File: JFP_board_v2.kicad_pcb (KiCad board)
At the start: 2 copper layers, 52.5 x 51.5 mm, 84 parts, among them J1 SPI2 external, J2 RX header, J3 I2C2 external, J4 UART4 external, J5 SWD conn, J6 ESC conn, J7 918-418K2023S40001, Q1 AO3400A, SW1 BOOT0, U1 TPS5430DDAR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

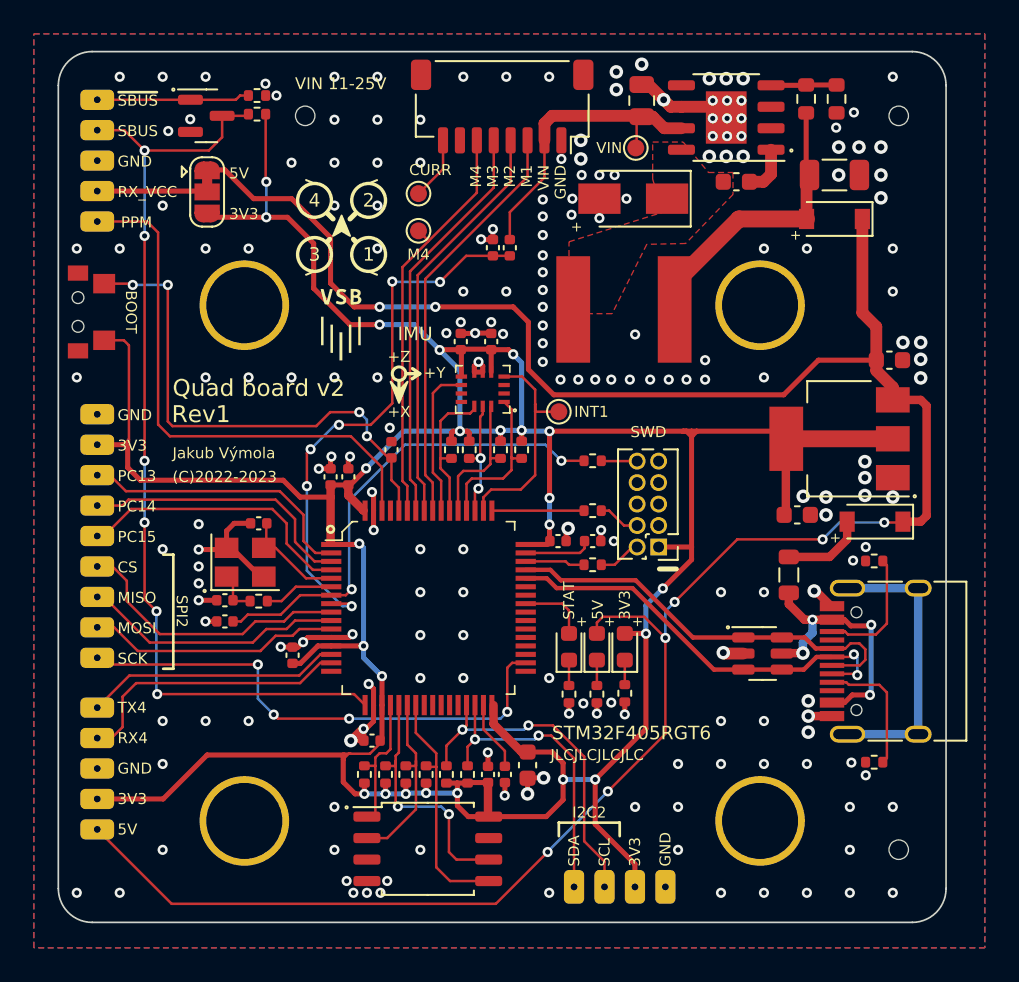
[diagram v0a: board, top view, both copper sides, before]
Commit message: Added HP203B pressure sensor
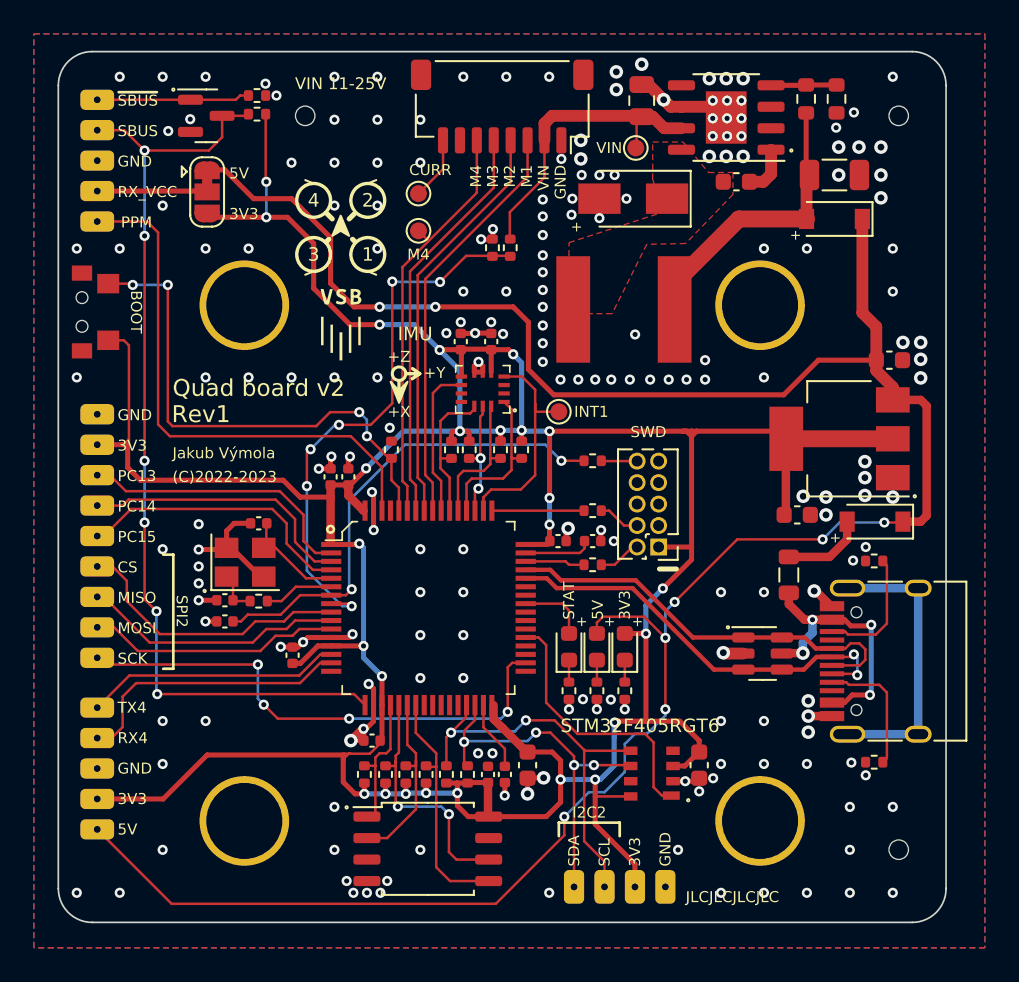
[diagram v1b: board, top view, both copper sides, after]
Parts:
- added C20: 4.7uF, Capacitor_SMD:C_0603_1608Metric, F.Cu at (163.4, 92.7)
- added U7: HP203B, _custom_footprints:LGA-8_3.6x3.8x0.9P, F.Cu at (160.6, 93.2)
- R10, R23, R24: footprint Capacitor_SMD:C_0402_1005Metric -> Resistor_SMD:R_0402_1005Metric
- R13, R15: value 100k -> 10k
- moved SW1 0.24 mm to (126.9, 65.9)
- moved R7 0.20 mm to (157.3, 88.3)
- moved R9 0.20 mm to (155.7, 88.3)
- moved R8 0.15 mm to (159.0, 88.3)
- moved REFQUAD 0.05 mm to (142.2, 60.9)
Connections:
- U3 pad 37: unconnected-(U3-Pad37) -> HP203B_INT1
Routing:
- net HP203B_INT1: track 0.00 -> 16.0 mm
- net +3V3: track 225.7 -> 234.8 mm, vias 24 -> 25
- net I2C2_SDA: track 17.9 -> 22.3 mm, vias 2 -> 4
- net I2C2_SCL: track 20.3 -> 24.3 mm
- net +5V: track 139.2 -> 140.1 mm
- net GND: track 43.7 -> 44.3 mm, vias 202 -> 201

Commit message: Production files
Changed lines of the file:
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@@
   (setup
     (stackup
-      (layer "F.SilkS" (type "Top Silk Screen"))
+      (layer "F.SilkS" (type "Top Silk Screen") (color "White"))
       (layer "F.Paste" (type "Top Solder Paste"))
-      (layer "F.Mask" (type "Top Solder Mask") (thickness 0.01))
+      (layer "F.Mask" (type "Top Solder Mask") (color "Green") (thickness 0.01))
       (layer "F.Cu" (type "copper") (thickness 0.035))
       (layer "dielectric 1" (type "core") (thickness 1.51) (material "FR4") (epsilon_r 4.5) (loss_tangent 0.02))
       (layer "B.Cu" (type "copper") (thickness 0.035))
-      (layer "B.Mask" (type "Bottom Solder Mask") (thickness 0.01))
+      (layer "B.Mask" (type "Bottom Solder Mask") (color "Green") (thickness 0.01))
       (layer "B.Paste" (type "Bottom Solder Paste"))
-      (layer "B.SilkS" (type "Bottom Silk Screen"))
+      (layer "B.SilkS" (type "Bottom Silk Screen") (color "White"))
       (copper_finish "None")
       (dielectric_constraints no)
@@
     (pad_to_mask_clearance 0.05)
     (pcbplotparams
-      (layerselection 0x00010fc_ffffffff)
+      (layerselection 0x000d0fc_ffffffff)
       (disableapertmacros false)
       (usegerberextensions false)
@@
       (svguseinch false)
       (svgprecision 6)
-      (excludeedgelayer true)
+      (excludeedgelayer false)
       (plotframeref false)
       (viasonmask false)
@@
       (sketchpadsonfab false)
       (subtractmaskfromsilk false)
-      (outputformat 1)
+      (outputformat 4)
       (mirror false)
       (drillshape 0)
       (scaleselection 1)
-      (outputdirectory "assembly/")
+      (outputdirectory "schematic/")
     )
   )
@@
     (effects (font (size 0.65 0.65) (thickness 0.16)) (justify left))
   )
-  (gr_text "VIN 11-25V" (at 142.2 52.4) (layer "F.SilkS")
+  (gr_text "VIN 11-25V" (at 142.225 52.85) (layer "F.SilkS")
     (effects (font (size 0.7 0.7) (thickness 0.16)))
   )
@@
     (effects (font (size 1 1) (thickness 0.2)) (justify left))
   )
-  (gr_text "JLCJLCJLCJLC" (at 162.6 100.5) (layer "F.SilkS")
+  (gr_text "JLCJLCJLCJLC" (at 162.625 99.6) (layer "F.SilkS")
     (effects (font (size 0.65 0.65) (thickness 0.16)) (justify left))
   )
@@
   (segment (start 141.64 84.65) (end 139.75 84.65) (width 0.15) (layer "F.Cu") (net 21))
   (segment (start 138.35 85.05) (end 137.45 85.95) (width 0.15) (layer "F.Cu") (net 21))
-  (segment (start 137.65025 89.12475) (end 138.4755 89.95) (width 0.15) (layer "F.Cu") (net 22))
+  (segment (start 138.4755 89.95) (end 142.7 89.95) (width 0.15) (layer "F.Cu") (net 22))
+  (segment (start 137.88775 89.36225) (end 138.4755 89.95) (width 0.15) (layer "F.Cu") (net 22))
   (segment (start 152.34 86.65) (end 153.14 86.65) (width 0.15) (layer "F.Cu") (net 22))
   (segment (start 128.2 86.75) (end 137.3 86.75) (width 0.15) (layer "F.Cu") (net 22))
   (segment (start 152.075 89.55) (end 152.075 86.915) (width 0.15) (layer "F.Cu") (net 22))
-  (segment (start 138.4755 89.95) (end 142.7 89.95) (width 0.15) (layer "F.Cu") (net 22))
   (segment (start 152.075 86.915) (end 152.34 86.65) (width 0.15) (layer "F.Cu") (net 22))
   (via (at 152.075 89.55) (size 0.6) (drill 0.3) (layers "F.Cu" "B.Cu") (net 22))
-  (via (at 137.65025 89.12475) (size 0.6) (drill 0.3) (layers "F.Cu" "B.Cu") (net 22))
+  (via (at 137.88775 89.36225) (size 0.6) (drill 0.3) (layers "F.Cu" "B.Cu") (net 22))
   (via (at 137.3 86.75) (size 0.6) (drill 0.3) (layers "F.Cu" "B.Cu") (net 22))
   (via (at 142.7 89.95) (size 0.6) (drill 0.3) (layers "F.Cu" "B.Cu") (net 22))
   (segment (start 152.075 89.55) (end 151.675 89.95) (width 0.15) (layer "B.Cu") (net 22))
-  (segment (start 137.65025 89.12475) (end 137.3 88.7745) (width 0.15) (layer "B.Cu") (net 22))
   (segment (start 137.3 88.7745) (end 137.3 86.75) (width 0.15) (layer "B.Cu") (net 22))
+  (segment (start 137.88775 89.36225) (end 137.3 88.7745) (width 0.15) (layer "B.Cu") (net 22))
   (segment (start 151.675 89.95) (end 142.7 89.95) (width 0.15) (layer "B.Cu") (net 22))
   (segment (start 139 78.4) (end 138.15 77.55) (width 0.15) (layer "F.Cu") (net 23))
@@
   (segment (start 142.8 73.25) (end 144.64 75.09) (width 0.15) (layer "F.Cu") (net 27))
   (segment (start 144.64 75.09) (end 144.64 77.65) (width 0.15) (layer "F.Cu") (net 27))
+  (segment (start 143.215 88.725) (end 143.64 89.15) (width 0.15) (layer "F.Cu") (net 28))
   (segment (start 131.306233 83.6) (end 130.6 82.893767) (width 0.15) (layer "F.Cu") (net 28))
   (segment (start 136.64 54.3) (end 135.1875 54.3) (width 0.15) (layer "F.Cu") (net 28))
   (segment (start 130.6 74.7) (end 130.6 61.4) (width 0.15) (layer "F.Cu") (net 28))
-  (segment (start 143.64 89.15) (end 142.99 88.5) (width 0.15) (layer "F.Cu") (net 28))
   (segment (start 130.6 56.35) (end 134.4 56.35) (width 0.15) (layer "F.Cu") (net 28))
   (segment (start 129.4 55.15) (end 130.6 56.35) (width 0.15) (layer "F.Cu") (net 28))
   (segment (start 135.1875 55.5625) (end 135.1875 54.3) (width 0.15) (layer "F.Cu") (net 28))
-  (segment (start 142.99 88.5) (end 131.35 88.5) (width 0.15) (layer "F.Cu") (net 28))
+  (segment (start 131.45 88.725) (end 143.215 88.725) (width 0.15) (layer "F.Cu") (net 28))
   (segment (start 127.8 55.15) (end 129.4 55.15) (width 0.15) (layer "F.Cu") (net 28))
   (segment (start 134.4 56.35) (end 135.1875 55.5625) (width 0.15) (layer "F.Cu") (net 28))
   (segment (start 130.6 82.893767) (end 130.6 78.35) (width 0.15) (layer "F.Cu") (net 28))
+  (segment (start 131.4 88.775) (end 131.45 88.725) (width 0.15) (layer "F.Cu") (net 28))
   (via (at 130.6 78.35) (size 0.6) (drill 0.3) (layers "F.Cu" "B.Cu") (net 28))
   (via (at 131.306233 83.6) (size 0.6) (drill 0.3) (layers "F.Cu" "B.Cu") (net 28))
@@
   (via (at 130.6 56.35) (size 0.6) (drill 0.3) (layers "F.Cu" "B.Cu") (net 28))
   (via (at 130.6 61.4) (size 0.6) (drill 0.3) (layers "F.Cu" "B.Cu") (net 28))
-  (via (at 131.35 88.5) (size 0.6) (drill 0.3) (layers "F.Cu" "B.Cu") (net 28))
+  (via (at 131.4 88.775) (size 0.6) (drill 0.3) (layers "F.Cu" "B.Cu") (net 28))
+  (segment (start 131.3 83.606233) (end 131.306233 83.6) (width 0.15) (layer "B.Cu") (net 28))
   (segment (start 130.6 56.35) (end 130.6 61.4) (width 0.15) (layer "B.Cu") (net 28))
-  (segment (start 131.35 88.5) (end 131.3 88.45) (width 0.15) (layer "B.Cu") (net 28))
+  (segment (start 131.3 88.675) (end 131.3 83.606233) (width 0.15) (layer "B.Cu") (net 28))
+  (segment (start 131.4 88.775) (end 131.3 88.675) (width 0.15) (layer "B.Cu") (net 28))
   (segment (start 130.6 74.7) (end 130.6 78.35) (width 0.15) (layer "B.Cu") (net 28))
-  (segment (start 131.3 88.45) (end 131.3 83.606233) (width 0.15) (layer "B.Cu") (net 28))
-  (segment (start 131.3 83.606233) (end 131.306233 83.6) (width 0.15) (layer "B.Cu") (net 28))
   (segment (start 136 53.35) (end 136.25 53.1) (width 0.15) (layer "F.Cu") (net 29))
   (segment (start 136.25 53.1) (end 136.74 53.1) (width 0.15) (layer "F.Cu") (net 29))
@@
   (segment (start 139.75 87.4) (end 129.7 87.4) (width 0.15) (layer "F.Cu") (net 32))
   (segment (start 141.64 86.65) (end 140.99427 86.65) (width 0.15) (layer "F.Cu") (net 33))
-  (segment (start 140.99427 86.65) (end 139.79427 87.85) (width 0.15) (layer "F.Cu") (net 33))
   (segment (start 129.3 88.65) (end 129.3 90.45) (width 0.15) (layer "F.Cu") (net 33))
-  (segment (start 139.79427 87.85) (end 130.1 87.85) (width 0.15) (layer "F.Cu") (net 33))
+  (segment (start 139.69427 87.95) (end 130 87.95) (width 0.15) (layer "F.Cu") (net 33))
+  (segment (start 130 87.95) (end 129.3 88.65) (width 0.15) (layer "F.Cu") (net 33))
   (segment (start 129.3 90.45) (end 128.65 91.1) (width 0.15) (layer "F.Cu") (net 33))
-  (segment (start 130.1 87.85) (end 129.3 88.65) (width 0.15) (layer "F.Cu") (net 33))
+  (segment (start 140.99427 86.65) (end 139.69427 87.95) (width 0.15) (layer "F.Cu") (net 33))
   (segment (start 157.61 80.85) (end 158.4 80.85) (width 0.15) (layer "F.Cu") (net 34))
   (segment (start 158.4 80.85) (end 159.45 79.8) (width 0.15) (layer "F.Cu") (net 34))
